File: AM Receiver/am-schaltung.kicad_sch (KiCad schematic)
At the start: 71 parts, among them IC1 NE612, IC2 NE612, IC3 74HC74, IC4 TDA1072, IC5 74HCT4046, IC6 L78L05_SO8, IC7 L78L05_SO8, P1 50k, Q1 Q_NJFET_DGS, Q2 Q_NJFET_DGS, Q3 BC547, Q4 BC547, Q5 BC557

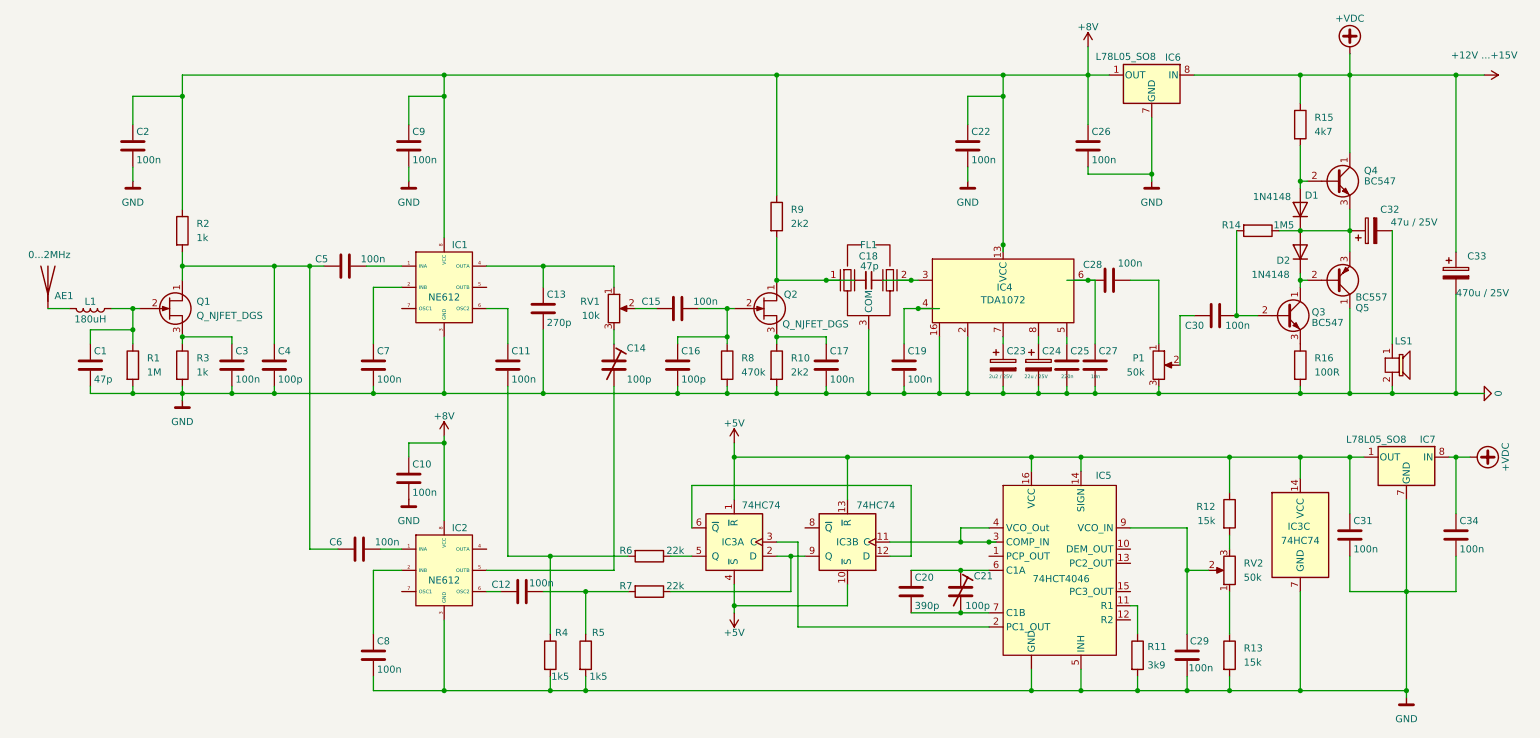
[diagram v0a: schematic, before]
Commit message: Finished ECG Schematic and finished laying out the PCB
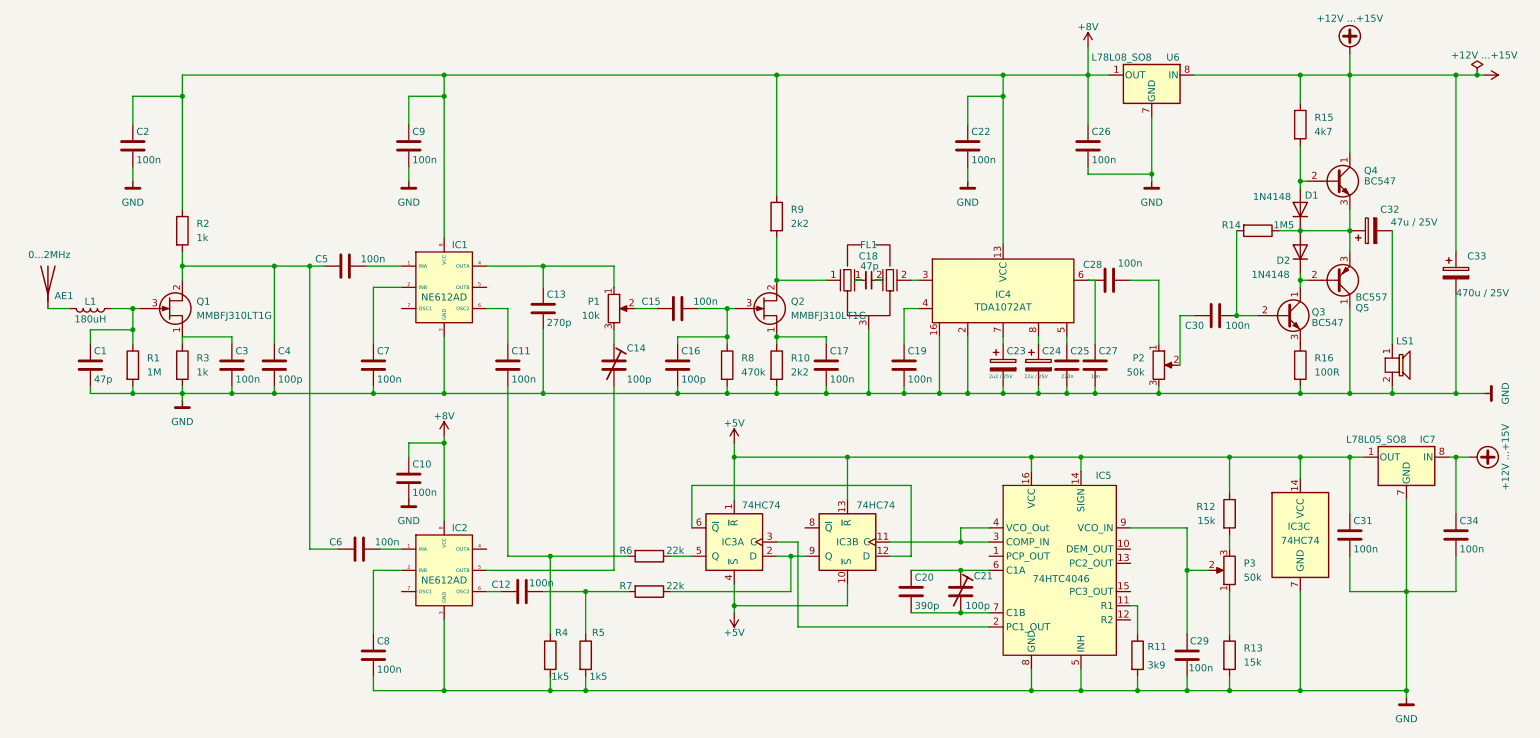
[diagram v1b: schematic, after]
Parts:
- AE1: footprint (none) -> Connector_PinHeader_2.54mm:PinHeader_1x02_P2.54mm_Vertical
- C1, C10, C11, C12, C13, C14, C15, C16, C17, C18, C19, C2, C20, C21, C22, C23, C24, C25, C26, C27, C28, C29, C3, C30, C31, C32, C33, C34, C4, C5, C6, C7, C8, C9: footprint (none) -> Capacitor_SMD:C_0603_1608Metric_Pad1.08x0.95mm_HandSolder
- IC1, IC2: value NE612 -> NE612AD; footprint (none) -> Package_SO:SOIC-8_3.9x4.9mm_P1.27mm; symbol Custom_RF_Mixer:NE612 -> AM_Receiver:NE612AD
- IC3: footprint (none) -> Package_SO:SOIC-14_3.9x8.7mm_P1.27mm
- IC4: value TDA1072 -> TDA1072AT; footprint (none) -> Package_SO:SOIC-16_3.9x9.9mm_P1.27mm
- IC5: value 74HCT4046 -> 74HTC4046; footprint (none) -> Package_SO:SOIC-16_3.9x9.9mm_P1.27mm; symbol AM_Receiver:74HCT4046 -> AM_Receiver:74HTC4046
- L1: footprint (none) -> Inductor_SMD:L_0201_0603Metric_Pad0.64x0.40mm_HandSolder
- P1: renamed from RV1; footprint (none) -> Potentiometer_SMD:Potentiometer_Bourns_3224W_Vertical
- P2: renamed from P1; footprint (none) -> Potentiometer_SMD:Potentiometer_Bourns_3224W_Vertical
- P3: renamed from RV2; footprint (none) -> Potentiometer_SMD:Potentiometer_Bourns_3224W_Vertical
- Q1, Q2: value Q_NJFET_DGS -> MMBFJ310LT1G; footprint (none) -> Package_TO_SOT_SMD:SOT-23; symbol Custom_Device:Q_NJFET_DGS -> AM_Receiver:MMBFJ310LT1G
- Q3, Q4, Q5: footprint Package_TO_SOT_THT:TO-92_Inline -> Package_TO_SOT_SMD:SOT-23
- R1, R10, R11, R12, R13, R14, R15, R16, R2, R3, R4, R5, R6, R7, R8, R9: footprint (none) -> Resistor_SMD:R_0603_1608Metric_Pad0.98x0.95mm_HandSolder
- U6: renamed from IC6; value L78L05_SO8 -> L78L08_SO8; symbol Regulator_Linear:L78L05_SO8 -> Regulator_Linear:L78L08_SO8
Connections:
- net at C4.1, C5.2, C6.2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: now also Q1.2 (D); no longer Q1.1 (D)
- net at C1.1, L1.1, R1.1: now also Q1.3 (G); no longer Q1.2 (G)
- net at C3.1, R3.1: now also Q1.1 (S); no longer Q1.3 (S)
- net at C15.1, C16.1, R8.1: now also Q2.3 (G); no longer Q2.2 (G)
- net at C18.2, FL1.1: no longer Q2.1 (D), R9.2
- net at FL1.2, IC4.3: no longer C18.1
- net at C17.1, R10.1: now also Q2.1 (S); no longer Q2.3 (S)
- net 0 renamed GND
- net GND: now also IC5.8 (GND); no longer IC5. (GND)
- new net: FL1.1, Q2.2 (D), R9.2
- new net: C18.1, FL1.2
